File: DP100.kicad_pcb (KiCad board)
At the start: 2 copper layers, 37 x 54 mm, 62 parts, among them J1 SMA CONNECTOR, J2 Conn_01x06, J3 Conn_02x06_Odd_Even, Q1 2N7002, U1 NCP1117-3.3_SOT223, U2 Si5351A-B-GT, U3 AD9215BRUZ, Y1 ABLS7M2-25.000MHZ-D2Y-T

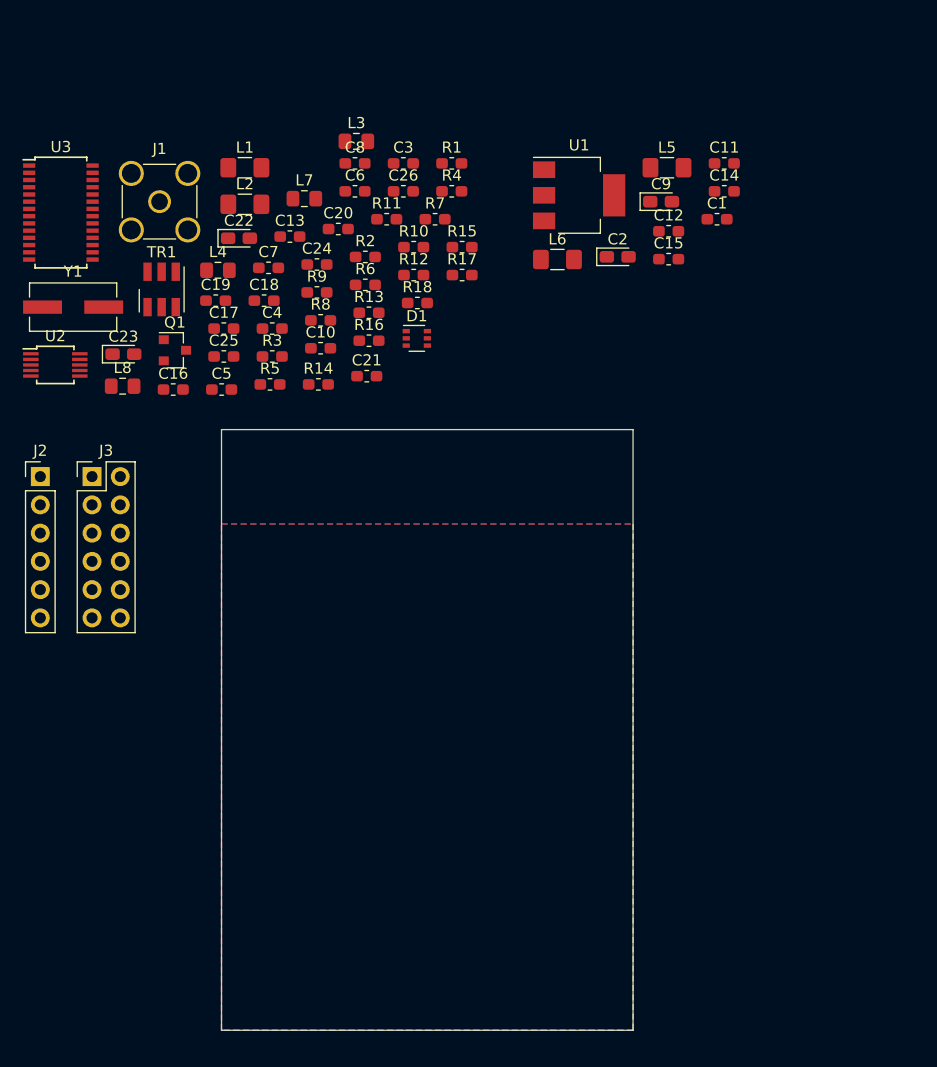
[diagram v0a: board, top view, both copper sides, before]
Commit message: Correcciones realizadas sobre el esquematico a partir de la revision realizada el dia 2/4 por Francisco Timez
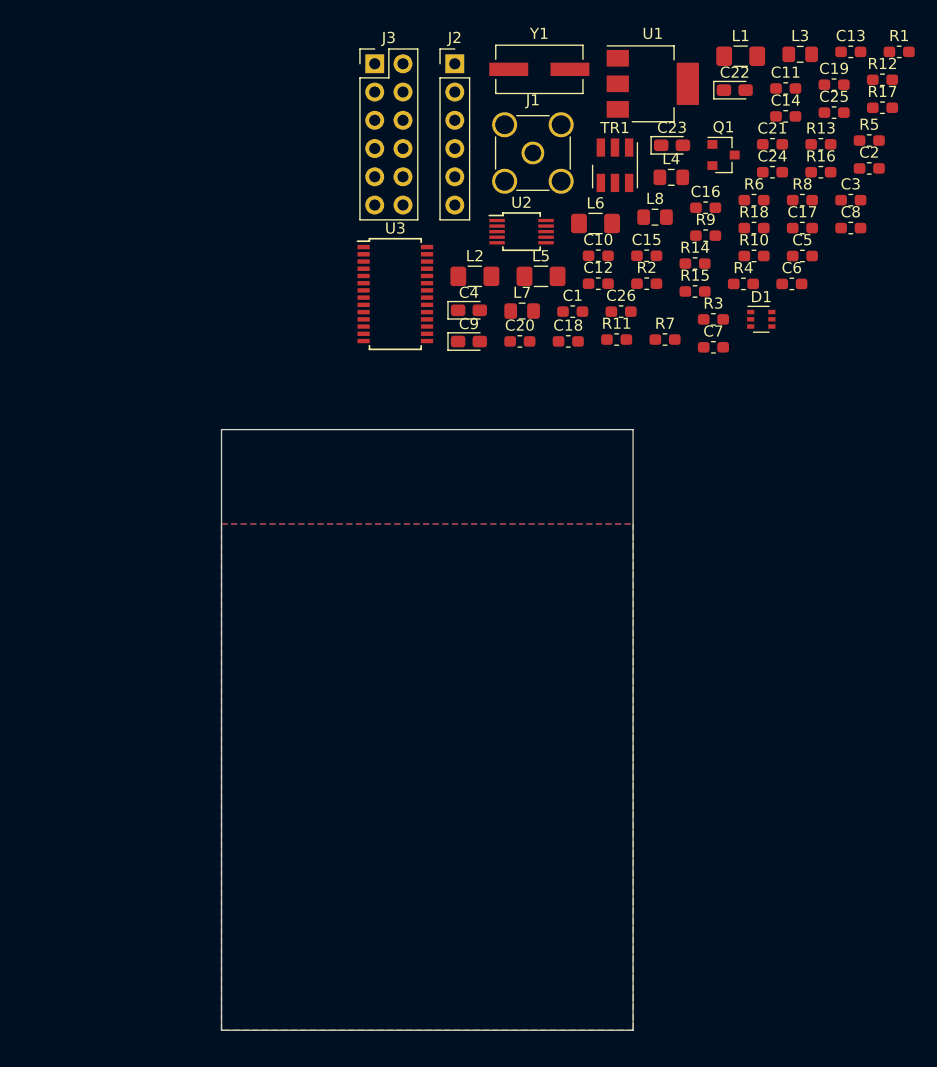
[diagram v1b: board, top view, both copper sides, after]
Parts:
- C2: value 10uF -> 100nF; footprint Capacitor_Tantalum_SMD:CP_EIA-2012-15_AVX-P_Pad1.30x1.05mm_HandSolder -> Capacitor_SMD:C_0603_1608Metric_Pad1.05x0.95mm_HandSolder
- C4: value 100nF -> 10uF; footprint Capacitor_SMD:C_0603_1608Metric_Pad1.05x0.95mm_HandSolder -> Capacitor_Tantalum_SMD:CP_EIA-2012-15_AVX-P_Pad1.30x1.05mm_HandSolder
- L1, L2: value 340nH -> 330nH
- Y1: value ABLS7M2-25.000MHZ-D2Y-T -> 25MHZ
- moved C25 59.1 mm to (161.5, 70.2)
- moved C19 58.9 mm to (161.5, 67.7)
- moved R5 58.2 mm to (164.6, 72.7)
- moved C5 53.6 mm to (158.6, 83.1)
- moved C13 53.1 mm to (163.0, 64.7)
- moved C17 52.8 mm to (158.6, 80.6)
- moved C23 52.8 mm to (146.9, 73.1)
- moved J2 52.6 mm to (127.4, 65.8)
- moved Q1 52.4 mm to (151.5, 74.0)
- moved C16 50.6 mm to (149.9, 78.8)
- moved L8 50.2 mm to (145.4, 79.6)
- moved Y1 47.1 mm to (135.0, 66.3)
- moved C22 46.5 mm to (152.5, 68.2)
- moved L1 45.7 mm to (153.1, 65.1)
- moved R12 45.7 mm to (165.8, 67.3)
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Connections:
- C2 pad 1: +5V -> Net-(C2-Pad1)
- C2 pad 2: GND -> filterIn+
- C26 pad 1: +3V3 -> GND
- C26 pad 2: GND -> +3V3
- C3 pad 2: filterIn+ -> filterIn-
- C4 pad 1: Net-(C4-Pad1) -> +5V
- C4 pad 2: filterIn- -> GND
- C5 pad 1: Net-(C3-Pad1) -> Net-(C2-Pad1)
- C5 pad 2: Net-(C4-Pad1) -> Net-(C3-Pad1)
- D1 pad 2: Net-(D1-Pad2) -> +3.3VA
- L1 pad 1: Net-(C3-Pad1) -> Net-(C2-Pad1)
- L2 pad 1: Net-(C4-Pad1) -> Net-(C3-Pad1)
- Q1 pad 3: Net-(Q1-Pad3) -> GND
- R14 pad 2: Net-(Q1-Pad3) -> GND
- R15 pad 2: Net-(C25-Pad1) -> Net-(R15-Pad2)
- R16 pad 1: Net-(C25-Pad1) -> Net-(R15-Pad2)
- R16 pad 2: Net-(R16-Pad2) -> Net-(C25-Pad1)
- R17 pad 1: Net-(R16-Pad2) -> Net-(C25-Pad1)
- R5 pad 1: Net-(D1-Pad2) -> +3.3VA
- U3 pad 2: Net-(C25-Pad1) -> GND
- U3 pad 3: Net-(Q1-Pad3) -> Net-(C21-Pad1)
- U3 pad 4: Net-(C21-Pad1) -> Net-(C25-Pad1)

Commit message: Cambio de etiquetas globales por jerarquicas en el esquematico. Posicionamiento de componentes y ruteo de PCB
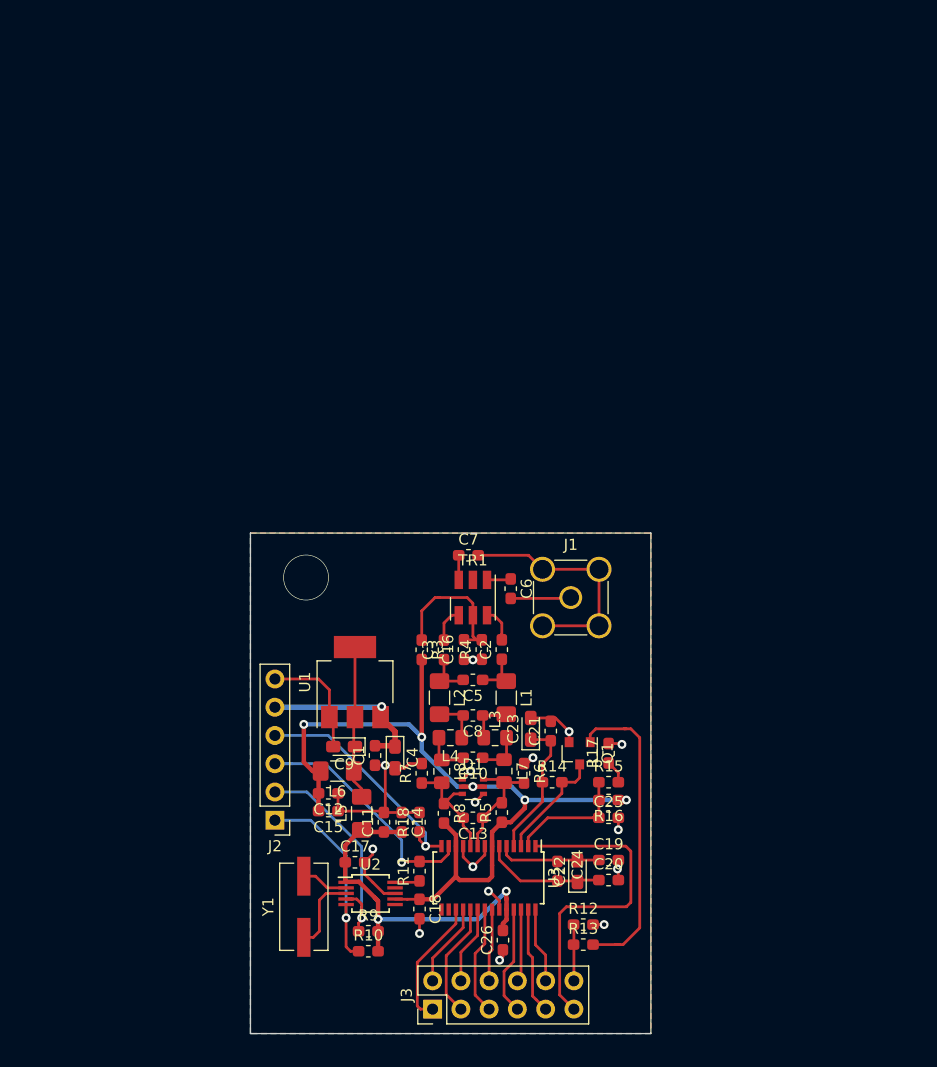
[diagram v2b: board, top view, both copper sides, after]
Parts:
- removed R1, R2: 0R, Resistor_SMD:R_0603_1608Metric_Pad1.05x0.95mm_HandSolder
- moved J3 85.1 mm to (125.4, 150.8), turned to 90 degrees
- moved R12 80.6 mm to (138.9, 143.2)
- moved Y1 78.2 mm to (113.8, 141.6), turned to 90 degrees
- moved C13 76.8 mm to (129.0, 133.6), turned to 180 degrees
- moved C11 75.2 mm to (121.0, 134.0), turned to 90 degrees
- moved R13 75.1 mm to (138.9, 145.0)
- moved C19 72.6 mm to (141.2, 137.4)
- moved C14 72.2 mm to (122.6, 134.0), turned to 270 degrees
- moved C22 71.6 mm to (138.4, 138.4), turned to 90 degrees
- moved R10 71.5 mm to (119.6, 145.6)
- moved J2 69.9 mm to (111.2, 133.8), turned to 180 degrees
- moved C17 69.8 mm to (118.4, 137.6)
- moved R9 69.5 mm to (119.6, 143.8)
- moved R5 68.9 mm to (131.6, 133.1), turned to 90 degrees
- moved L3 67.3 mm to (131.0, 126.4)
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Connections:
- net D0 renamed /D0
- net D1 renamed /D1
- net D2 renamed /D2
- net D3 renamed /D3
- net D4 renamed /D4
- net D5 renamed /D5
- net D6 renamed /D6
- net D7 renamed /D7
- net D8 renamed /D8
- net D9 renamed /D9
- net OR renamed /OR
- net Spam renamed /Spam
- net filterOut+ renamed /filterOut+
- net filterOut- renamed /filterOut-
- C2 pad 2: filterIn+ -> /filterIn+
- C3 pad 2: filterIn- -> /filterIn-
- J2 pad 1: PWDN -> /SDA
- J2 pad 2: SDA -> /SCL
- J2 pad 3: SCL -> /CLK
- J2 pad 4: CLK -> /PWDN
- Q1 pad 3: GND -> Net-(Q1-Pad3)
- R10 pad 1: SDA -> /SDA
- R11 pad 2: CLK -> /CLK
- R14 pad 2: GND -> Net-(Q1-Pad3)
- R15 pad 1: +3.3VA -> Net-(C25-Pad1)
- R16 pad 1: Net-(R15-Pad2) -> +3.3VA
- R17 pad 1: Net-(C25-Pad1) -> Net-(R15-Pad2)
- R18 pad 1: PWDN -> /PWDN
- R9 pad 1: SCL -> /SCL
- TR1 pad 4: Net-(R1-Pad1) -> /filterIn+
- TR1 pad 6: Net-(R2-Pad1) -> /filterIn-
- U2 pad 4: SCL -> /SCL
- U2 pad 5: SDA -> /SDA
- U3 pad 13: CLK -> /CLK
- U3 pad 14: PWDN -> /PWDN
- U3 pad 2: GND -> Net-(C25-Pad1)
- U3 pad 3: Net-(C21-Pad1) -> Net-(Q1-Pad3)
- U3 pad 4: Net-(C25-Pad1) -> Net-(C21-Pad1)
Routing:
- net +3.3VA: track 0.00 -> 75.0 mm, vias 0 -> 5
- net GND: track 0.00 -> 58.4 mm, vias 0 -> 15
- net +3V3: track 0.00 -> 33.7 mm, vias 0 -> 2
- net /OR: track 0.00 -> 29.3 mm
- net Net-(Q1-Pad1): track 0.00 -> 28.2 mm
- net /CLK: track 0.00 -> 23.0 mm, vias 0 -> 1
- net Net-(C7-Pad2): track 0.00 -> 21.5 mm
- net /PWDN: track 0.00 -> 21.3 mm, vias 0 -> 1
- net /SCL: track 0.00 -> 20.9 mm, vias 0 -> 1
- net /SDA: track 0.00 -> 18.4 mm, vias 0 -> 1
- net +5V: track 0.00 -> 14.6 mm, vias 0 -> 1
- net Net-(C9-Pad1): track 0.00 -> 13.8 mm
- net Net-(C16-Pad2): track 0.00 -> 13.5 mm
- net Net-(C21-Pad1): track 0.00 -> 12.6 mm
- net /D0: track 0.00 -> 11.6 mm
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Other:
- board size 37 x 54 mm -> 36 x 45 mm

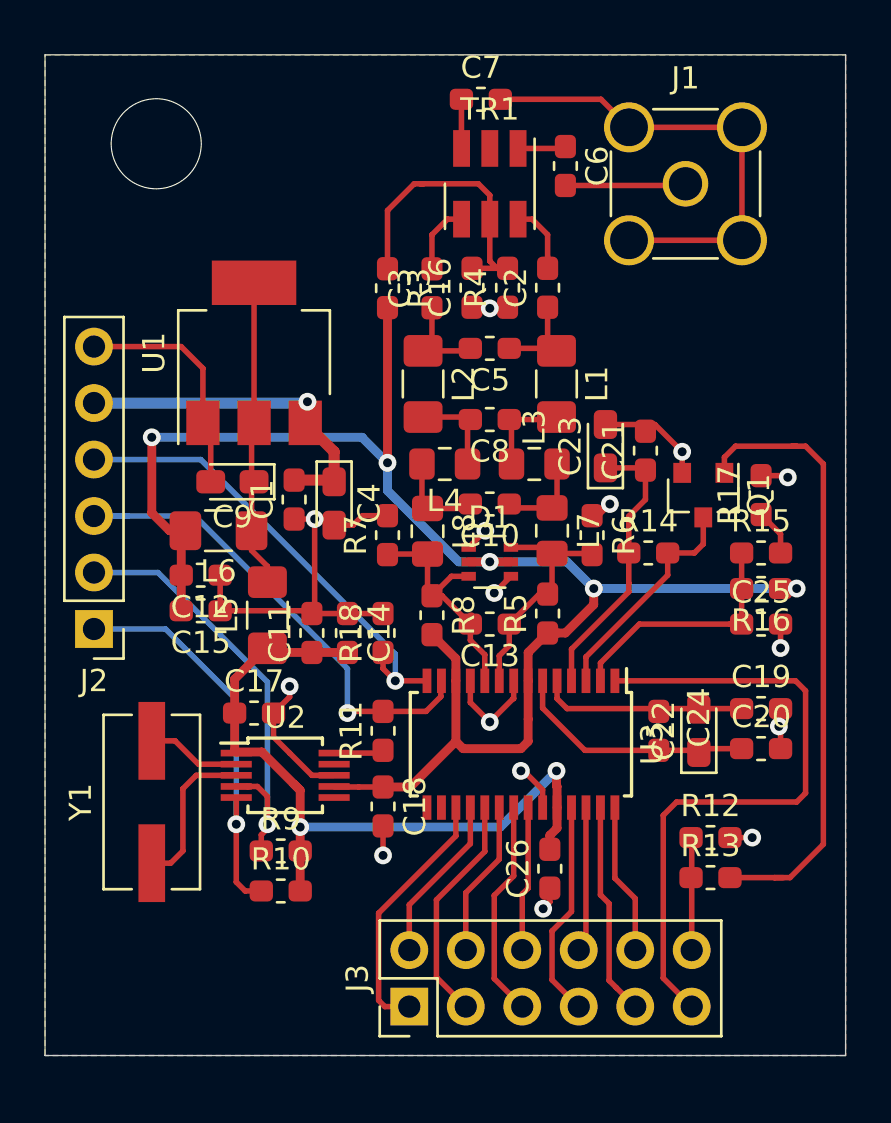
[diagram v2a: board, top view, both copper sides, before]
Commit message: Mascara de componentes posicionada correctamente Planos de tierra en ambas caras Reglas chequeadas segun fabricante Ernesto Mayer
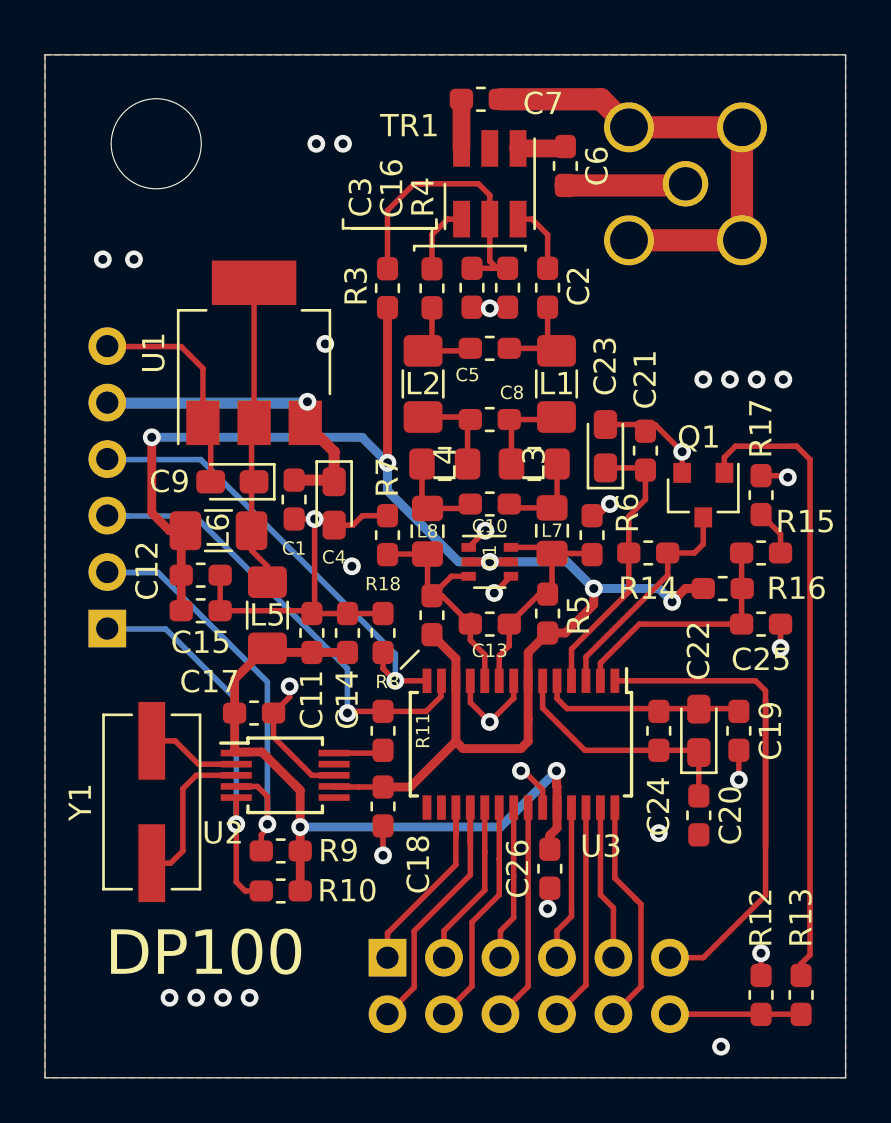
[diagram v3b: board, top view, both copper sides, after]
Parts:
- J1, J2, J3: moved to B.Cu
- moved R12 7.43 mm to (141.2, 150.3), turned to 90 degrees
- moved R13 6.67 mm to (143.0, 150.3), turned to 90 degrees
- moved C20 4.10 mm to (138.4, 142.2), turned to 270 degrees
- moved J3 2.41 mm to (124.4, 148.6), turned to 270 degrees
- moved R16 1.72 mm to (139.5, 132.0), turned to 0 degrees
- moved C19 1.41 mm to (140.2, 138.4), turned to 270 degrees
- moved J2 0.60 mm to (111.8, 133.8), turned to 0 degrees
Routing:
- net /D1: track 7.55 -> 12.5 mm
- net +3.3VA: track 75.0 -> 70.6 mm
- net /D9: track 6.79 -> 10.4 mm
- net /D5: track 6.52 -> 9.81 mm
- net /D3: track 7.03 -> 10.3 mm
- net /D7: track 6.54 -> 9.83 mm
- net /D2: track 10.4 -> 7.51 mm
- net /D4: track 9.83 -> 7.00 mm
- net /D6: track 9.81 -> 7.02 mm
- net /D8: track 9.60 -> 6.99 mm
- net /D0: track 11.6 -> 9.30 mm
- net /OR: track 29.3 -> 28.2 mm
- net /Spam: track 5.07 -> 6.02 mm
- net GND: track 58.4 -> 57.9 mm, vias 15 -> 31
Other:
- board size 36 x 45 mm -> 36 x 46 mm
- rule via_min_drill: 0.3 -> 0.4
- rule via_min_size: 0.4 -> 0.7
- board text added: "DP100"

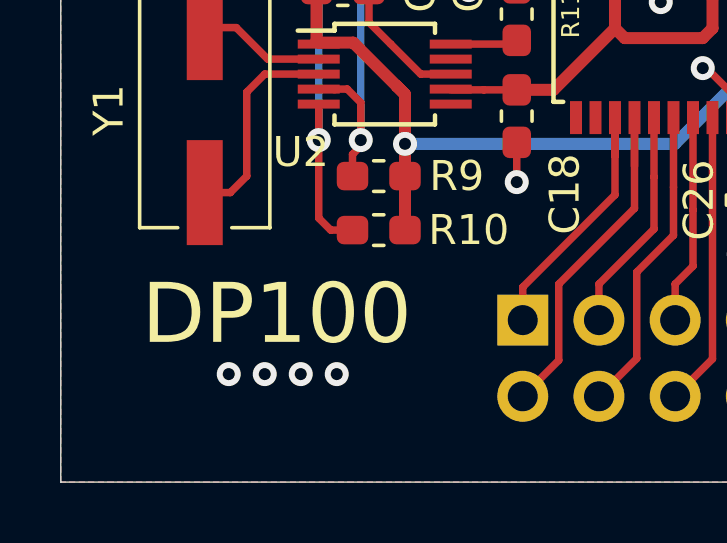
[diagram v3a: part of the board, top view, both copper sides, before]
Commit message: Se cambian las etiquetas jerarquicas por net labels.
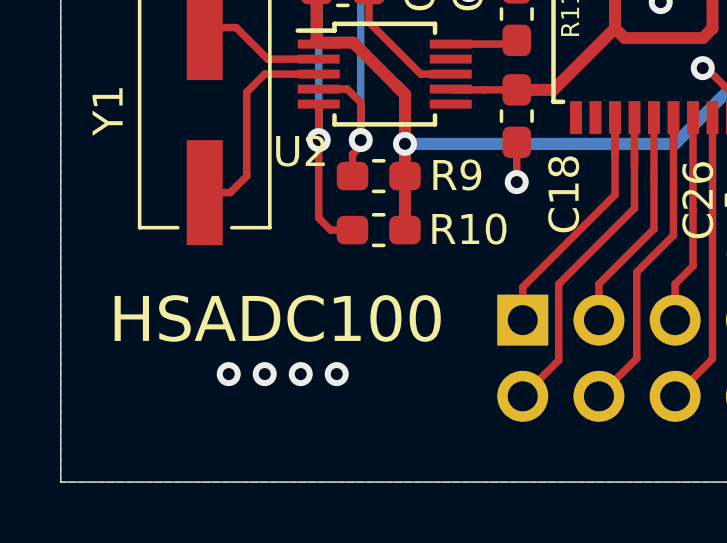
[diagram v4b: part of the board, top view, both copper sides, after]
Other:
- board text added: "HSADC100"
- board text removed: "DP100"
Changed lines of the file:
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@@
     )
   )
-  (gr_text DP100 (at 116.2 148.4) (layer F.SilkS)
-    (effects (font (size 2 2) (thickness 0.15)))
+  (gr_text HSADC100 (at 116.2 148.6) (layer F.SilkS)
+    (effects (font (size 1.5 1.5) (thickness 0.15)))
   )
   (gr_line (start 125 135.6) (end 125.8 134.8) (layer F.SilkS) (width 0.12))
